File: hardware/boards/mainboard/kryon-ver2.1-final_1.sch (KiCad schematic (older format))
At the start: 1 part

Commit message: mainboard
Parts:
- added D1, D2, D3, D4, D5, D6, D7, D8: 1N4148WS, Diodes_SMD:D_SOD-323, symbol Diode:1N4148WS
- added R33: 4.7k, Resistors_SMD:R_0805, symbol Device:R
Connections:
- net labels added: +3V3, GATE_1, GATE_2, GATE_3, GATE_4, MIDI_RX, MIDI_TX
- net labels removed: 3V3, RX, TX, VBAT
- wire segments 26 -> 31

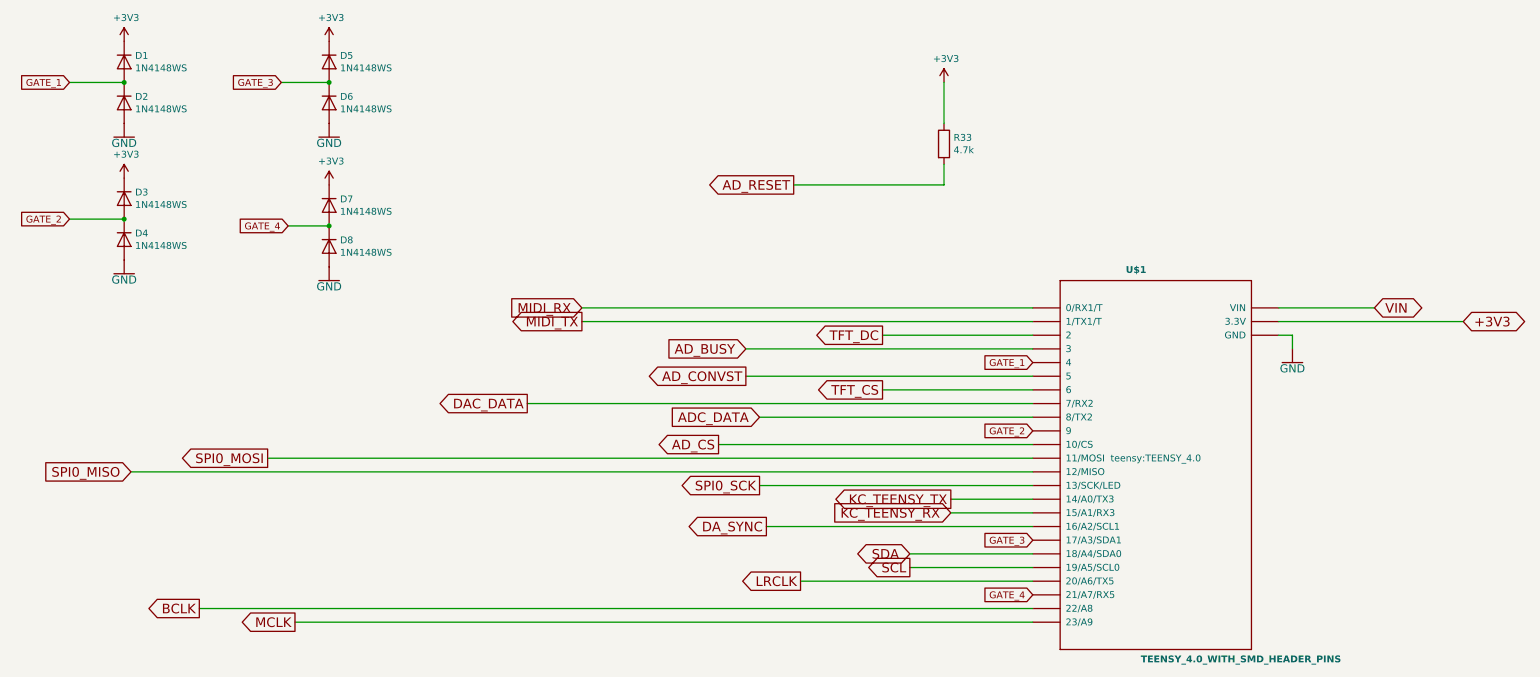
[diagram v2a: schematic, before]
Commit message: Mainboard: v1.5, changed diodes to 0805, corrected BCLK pin, moved LM340
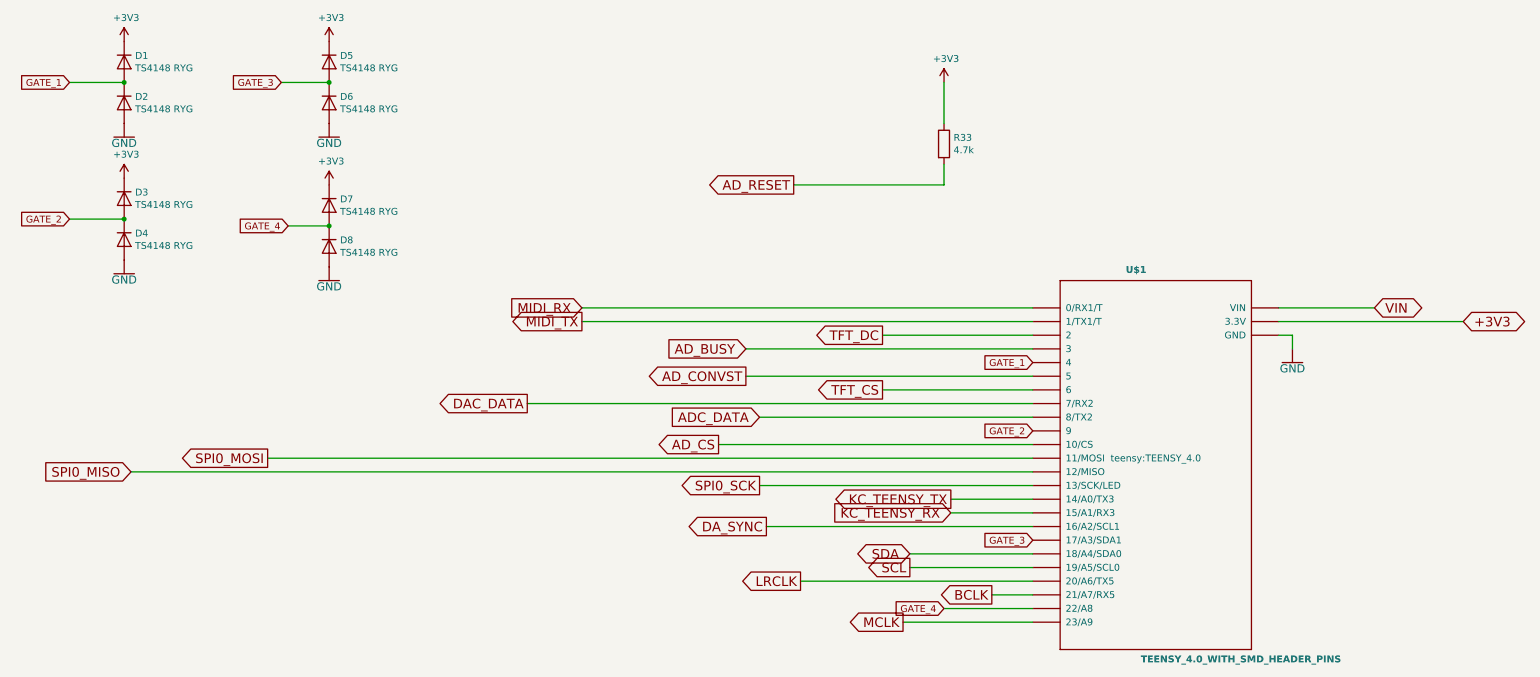
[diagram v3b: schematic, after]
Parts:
- D1, D2, D3, D4, D5, D6, D7, D8: value 1N4148WS -> TS4148 RYG; footprint Diodes_SMD:D_SOD-323 -> Diode_SMD:D_0805_2012Metric
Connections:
- net BCLK: now also U$1.21/A7 (21/A7/RX5); no longer U$1.22/A8
- net GATE_4: now also U$1.22/A8; no longer U$1.21/A7 (21/A7/RX5)
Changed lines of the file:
@@
 Text GLabel 5800 3700 0    70   Input ~ 0
 ADC_DATA
-Text GLabel 2400 5200 0    70   Output ~ 0
-MCLK
 Text GLabel 6100 4900 0    70   Output ~ 0
 LRCLK
 Text GLabel 4100 3600 0    70   Output ~ 0
 DAC_DATA
-Text GLabel 1700 5100 0    70   Output ~ 0
-BCLK
 Wire Wire Line
 	9700 3200 9700 3100
@@
 	6100 4900 7800 4900
 Wire Wire Line
-	1700 5100 7800 5100
-Wire Wire Line
 	6900 4700 7800 4700
 Wire Wire Line
@@
 Wire Wire Line
 	9600 3100 9700 3100
-Wire Wire Line
-	2400 5200 7800 5200
 $Comp
 L Device:R R33
@@
 Text GLabel 7800 4600 0    50   Input ~ 0
 GATE_3
-Text GLabel 7800 5000 0    50   Input ~ 0
-GATE_4
 Wire Wire Line
 	7150 1550 7150 1250
@@
 P 2650 2150
 F 0 "D7" V 2604 2230 50  0000 L CNN
-F 1 "1N4148WS" V 2695 2230 50  0000 L CNN
-F 2 "Diodes_SMD:D_SOD-323" H 2650 1975 50  0001 C CNN
+F 1 "TS4148 RYG" V 2695 2230 50  0000 L CNN
+F 2 "Diode_SMD:D_0805_2012Metric" H 2650 1975 50  0001 C CNN
 F 3 "https://www.vishay.com/docs/85751/1n4148ws.pdf" H 2650 2150 50  0001 C CNN
 	1    2650 2150
@@
 P 2650 2450
 F 0 "D8" V 2604 2530 50  0000 L CNN
-F 1 "1N4148WS" V 2695 2530 50  0000 L CNN
-F 2 "Diodes_SMD:D_SOD-323" H 2650 2275 50  0001 C CNN
+F 1 "TS4148 RYG" V 2695 2530 50  0000 L CNN
+F 2 "Diode_SMD:D_0805_2012Metric" H 2650 2275 50  0001 C CNN
 F 3 "https://www.vishay.com/docs/85751/1n4148ws.pdf" H 2650 2450 50  0001 C CNN
 	1    2650 2450
@@
 P 2650 1100
 F 0 "D5" V 2604 1180 50  0000 L CNN
-F 1 "1N4148WS" V 2695 1180 50  0000 L CNN
-F 2 "Diodes_SMD:D_SOD-323" H 2650 925 50  0001 C CNN
+F 1 "TS4148 RYG" V 2695 1180 50  0000 L CNN
+F 2 "Diode_SMD:D_0805_2012Metric" H 2650 925 50  0001 C CNN
 F 3 "https://www.vishay.com/docs/85751/1n4148ws.pdf" H 2650 1100 50  0001 C CNN
 	1    2650 1100
@@
 P 2650 1400
 F 0 "D6" V 2604 1480 50  0000 L CNN
-F 1 "1N4148WS" V 2695 1480 50  0000 L CNN
-F 2 "Diodes_SMD:D_SOD-323" H 2650 1225 50  0001 C CNN
+F 1 "TS4148 RYG" V 2695 1480 50  0000 L CNN
+F 2 "Diode_SMD:D_0805_2012Metric" H 2650 1225 50  0001 C CNN
 F 3 "https://www.vishay.com/docs/85751/1n4148ws.pdf" H 2650 1400 50  0001 C CNN
 	1    2650 1400
@@
 P 1150 1100
 F 0 "D1" V 1104 1180 50  0000 L CNN
-F 1 "1N4148WS" V 1195 1180 50  0000 L CNN
-F 2 "Diodes_SMD:D_SOD-323" H 1150 925 50  0001 C CNN
+F 1 "TS4148 RYG" V 1195 1180 50  0000 L CNN
+F 2 "Diode_SMD:D_0805_2012Metric" H 1150 925 50  0001 C CNN
 F 3 "https://www.vishay.com/docs/85751/1n4148ws.pdf" H 1150 1100 50  0001 C CNN
 	1    1150 1100
@@
 P 1150 1400
 F 0 "D2" V 1104 1480 50  0000 L CNN
-F 1 "1N4148WS" V 1195 1480 50  0000 L CNN
-F 2 "Diodes_SMD:D_SOD-323" H 1150 1225 50  0001 C CNN
+F 1 "TS4148 RYG" V 1195 1480 50  0000 L CNN
+F 2 "Diode_SMD:D_0805_2012Metric" H 1150 1225 50  0001 C CNN
 F 3 "https://www.vishay.com/docs/85751/1n4148ws.pdf" H 1150 1400 50  0001 C CNN
 	1    1150 1400
@@
 P 1150 2100
 F 0 "D3" V 1104 2180 50  0000 L CNN
-F 1 "1N4148WS" V 1195 2180 50  0000 L CNN
-F 2 "Diodes_SMD:D_SOD-323" H 1150 1925 50  0001 C CNN
+F 1 "TS4148 RYG" V 1195 2180 50  0000 L CNN
+F 2 "Diode_SMD:D_0805_2012Metric" H 1150 1925 50  0001 C CNN
 F 3 "https://www.vishay.com/docs/85751/1n4148ws.pdf" H 1150 2100 50  0001 C CNN
 	1    1150 2100
@@
 P 1150 2400
 F 0 "D4" V 1104 2480 50  0000 L CNN
-F 1 "1N4148WS" V 1195 2480 50  0000 L CNN
-F 2 "Diodes_SMD:D_SOD-323" H 1150 2225 50  0001 C CNN
+F 1 "TS4148 RYG" V 1195 2480 50  0000 L CNN
+F 2 "Diode_SMD:D_0805_2012Metric" H 1150 2225 50  0001 C CNN
 F 3 "https://www.vishay.com/docs/85751/1n4148ws.pdf" H 1150 2400 50  0001 C CNN
 	1    1150 2400
@@
 Text GLabel 2350 2300 0    50   Input ~ 0
 GATE_4
+Text GLabel 7500 5000 0    70   Output ~ 0
+BCLK
+Wire Wire Line
+	6850 5200 7800 5200
+Text GLabel 6850 5200 0    70   Output ~ 0
+MCLK
+Text GLabel 7150 5100 0    50   Input ~ 0
+GATE_4
+Wire Wire Line
+	7150 5100 7800 5100
+Wire Wire Line
+	7500 5000 7800 5000
 $EndSCHEMATC

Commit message: mainboard v1.6
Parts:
- added U2: PCA9536, Package_SO:TSSOP-8_3x3mm_P0.65mm, symbol Mainboard-eagle-import:PCA9536
- U$1: footprint teensy:TEENSY_4.0 -> Mainboard:TEENSY_4.0_WITH_SMD_HEADER_PINS; symbol Mainboard-eagle-import:TEENSY_4.0 -> Mainboard-eagle-import:TEENSY_4.0_WITH_SMD_HEADER_PINS
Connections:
- net +3V3: no longer D1.1 (K), D3.1 (K), D5.1 (K), D7.1 (K)
- net AD_RESET: now also U$1.4
- net GATE_1: now also U2.1 (IO0); no longer U$1.4
- net GATE_2: now also U2.2 (IO1); no longer U$1.9
- net GATE_3: now also U2.3 (IO2); no longer U$1.17/A3 (17/A3/SDA1)
- net GATE_4: now also U2.5 (IO3); no longer U$1.22/A8
- net SCL: now also U2.6 (SCL)
- net SDA: now also U2.7 (SDA)
- net VIN: now also D1.1 (K), D3.1 (K), D5.1 (K), D7.1 (K), U2.8 (VDD)
- new net BUS_TEENSY_RX: U$1.28 (28/RX7)
- new net BUS_TEENSY_TX: U$1.29 (29/TX7)
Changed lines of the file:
@@
 DA_SYNC
 $Comp
-L Mainboard-eagle-import:TEENSY_4.0 U$1
+L Mainboard-eagle-import:TEENSY_4.0_WITH_SMD_HEADER_PINS U$1
 U 1 1 2AECCF64
 P 8700 4000
 F 0 "U$1" H 8480 5350 50  0000 L BNB
 F 1 "TEENSY_4.0_WITH_SMD_HEADER_PINS" H 8590 2500 50  0000 L BNB
-F 2 "teensy:TEENSY_4.0" H 8700 4000 50  0000 C CNN
+F 2 "Mainboard:TEENSY_4.0_WITH_SMD_HEADER_PINS" H 8700 4000 50  0000 C CNN
 F 3 "" H 8700 4000 50  0001 C CNN
 	1    8700 4000
@@
 Wire Wire Line
 	9600 3100 9700 3100
-$Comp
-L Device:R R33
-U 1 1 5D90FA7F
-P 7150 1700
-F 0 "R33" H 7220 1746 50  0000 L CNN
-F 1 "4.7k" H 7220 1655 50  0000 L CNN
-F 2 "Resistors_SMD:R_0805" V 7080 1700 50  0001 C CNN
-F 3 "~" H 7150 1700 50  0001 C CNN
-	1    7150 1700
-	1    0    0    -1
-$EndComp
 $Comp
 L power:+3V3 #PWR0103
@@
 Wire Wire Line
 	7150 2000 7150 1850
-Text GLabel 7800 3300 0    50   Input ~ 0
+Text GLabel 8200 2000 0    50   Input ~ 0
 GATE_1
-Text GLabel 7800 3800 0    50   Input ~ 0
+Text GLabel 8200 2100 0    50   Input ~ 0
 GATE_2
-Text GLabel 7800 4600 0    50   Input ~ 0
+Text GLabel 8200 2200 0    50   Input ~ 0
 GATE_3
 Wire Wire Line
@@
 	1    1150 2400
 	0    1    1    0
-$EndComp
-$Comp
-L power:+3V3 #PWR01
-U 1 1 5D9A4421
-P 1150 950
-F 0 "#PWR01" H 1150 800 50  0001 C CNN
-F 1 "+3V3" H 1165 1123 50  0000 C CNN
-F 2 "" H 1150 950 50  0001 C CNN
-F 3 "" H 1150 950 50  0001 C CNN
-	1    1150 950
-	1    0    0    -1
-$EndComp
-$Comp
-L power:+3V3 #PWR03
-U 1 1 5D9A4CAB
-P 2650 950
-F 0 "#PWR03" H 2650 800 50  0001 C CNN
-F 1 "+3V3" H 2665 1123 50  0000 C CNN
-F 2 "" H 2650 950 50  0001 C CNN
-F 3 "" H 2650 950 50  0001 C CNN
-	1    2650 950
-	1    0    0    -1
-$EndComp
-$Comp
-L power:+3V3 #PWR02
-U 1 1 5D9A56BC
-P 1150 1950
-F 0 "#PWR02" H 1150 1800 50  0001 C CNN
-F 1 "+3V3" H 1165 2123 50  0000 C CNN
-F 2 "" H 1150 1950 50  0001 C CNN
-F 3 "" H 1150 1950 50  0001 C CNN
-	1    1150 1950
-	1    0    0    -1
-$EndComp
-$Comp
-L power:+3V3 #PWR04
-U 1 1 5D9A5E04
-P 2650 2000
-F 0 "#PWR04" H 2650 1850 50  0001 C CNN
-F 1 "+3V3" H 2665 2173 50  0000 C CNN
-F 2 "" H 2650 2000 50  0001 C CNN
-F 3 "" H 2650 2000 50  0001 C CNN
-	1    2650 2000
-	1    0    0    -1
 $EndComp
 $Comp
@@
 Text GLabel 6850 5200 0    70   Output ~ 0
 MCLK
-Text GLabel 7150 5100 0    50   Input ~ 0
+Text GLabel 8800 2300 2    50   Input ~ 0
 GATE_4
 Wire Wire Line
-	7150 5100 7800 5100
-Wire Wire Line
 	7500 5000 7800 5000
+$Comp
+L Device:R R33
+U 1 1 5D90FA7F
+P 7150 1700
+F 0 "R33" H 7220 1746 50  0000 L CNN
+F 1 "4.7k" H 7220 1655 50  0000 L CNN
+F 2 "Resistors_SMD:R_0805" V 7080 1700 50  0001 C CNN
+F 3 "~" H 7150 1700 50  0001 C CNN
+	1    7150 1700
+	1    0    0    -1
+$EndComp
+$Comp
+L Mainboard-eagle-import:PCA9536 U2
+U 1 1 5DF732B1
+P 8500 2150
+F 0 "U2" H 8500 2525 50  0000 C CNN
+F 1 "PCA9536" H 8500 2434 50  0000 C CNN
+F 2 "Package_SO:TSSOP-8_3x3mm_P0.65mm" H 8500 2150 50  0001 C CNN
+F 3 "" H 8500 2150 50  0001 C CNN
+	1    8500 2150
+	1    0    0    -1
+$EndComp
+$Comp
+L Mainboard-eagle-import:GND #GND0101
+U 1 1 5DF7872C
+P 8200 2400
+F 0 "#GND0101" H 8200 2400 50  0001 C CNN
+F 1 "GND" H 8200 2390 59  0000 C TNN
+F 2 "" H 8200 2400 50  0001 C CNN
+F 3 "" H 8200 2400 50  0001 C CNN
+	1    8200 2400
+	1    0    0    -1
+$EndComp
+Text Label 8800 2200 0    50   ~ 0
+SCL
+Text Label 8800 2100 0    50   ~ 0
+SDA
+Text Label 8800 2000 0    50   ~ 0
+VIN
+Wire Wire Line
+	7800 3300 7150 3300
+Wire Wire Line
+	7150 3300 7150 2000
+Connection ~ 7150 2000
+Text Label 1150 950  0    50   ~ 0
+VIN
+Text Label 2650 950  0    50   ~ 0
+VIN
+Text Label 2650 2000 0    50   ~ 0
+VIN
+Text Label 1150 1950 0    50   ~ 0
+VIN
+Wire Wire Line
+	9600 4100 10000 4100
+Wire Wire Line
+	9600 4200 10000 4200
+Text GLabel 10000 4100 2    50   Input ~ 0
+BUS_TEENSY_RX
+Text GLabel 10000 4200 2    50   Input ~ 0
+BUS_TEENSY_TX
 $EndSCHEMATC
